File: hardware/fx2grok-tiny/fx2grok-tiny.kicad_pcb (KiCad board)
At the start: 2 copper layers, 13 x 13 mm, 28 parts, among them IC1 CY7C68013A-56, P1 CONN_01X05, P2 CONN_01X05, U1 MICRO-USB-B-SMD, U2 MIC5319, Y1 24MHz

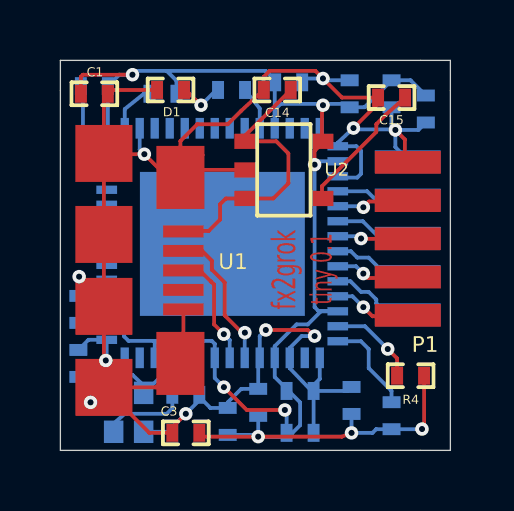
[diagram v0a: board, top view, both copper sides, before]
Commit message: Use rounded PCB edges, minor other improvements.
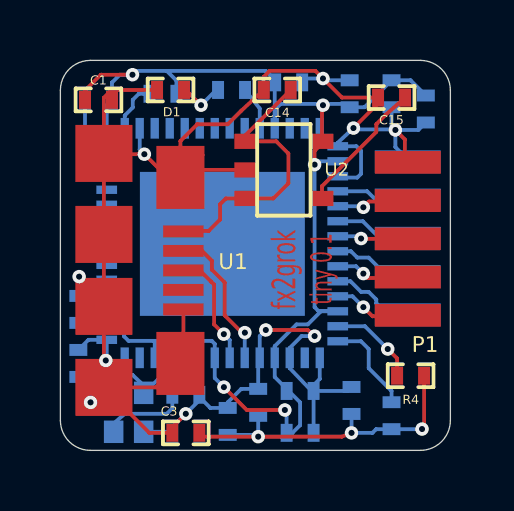
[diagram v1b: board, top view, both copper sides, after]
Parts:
- moved R1 0.48 mm to (69.0, 39.1)
- moved C1 0.25 mm to (69.0, 39.1)
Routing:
- net /WAKEUP: track 3.18 -> 2.63 mm
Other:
- outline, holes or cut-outs redrawn

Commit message: Add 0/1/GND pin markings on the 5x2 1.27mm connector.
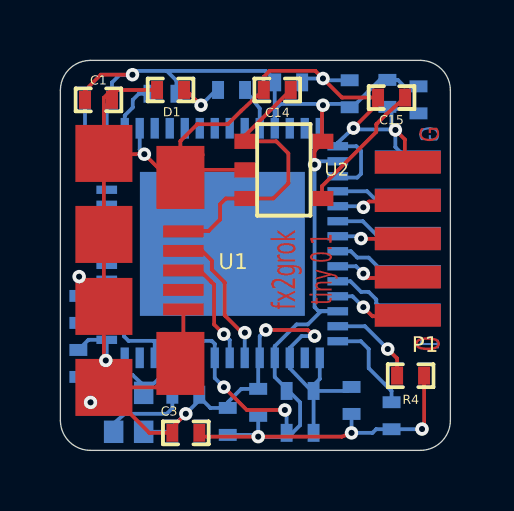
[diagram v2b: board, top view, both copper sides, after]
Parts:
- moved C16 0.39 mm to (79.6, 39.1)
- moved C10 0.14 mm to (78.6, 38.8)
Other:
- board text added: "0"
- board text added: "1"
- board text added: "G"
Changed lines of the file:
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@@
     (links 85)
     (no_connects 0)
-    (area 50.03038 32.773983 88.390762 61.842831)
+    (area 67.688459 37.736499 80.713861 50.761901)
     (thickness 0.8)
-    (drawings 12)
-    (tracks 346)
+    (drawings 16)
+    (tracks 356)
     (zones 0)
     (modules 28)
@@
   )
   (module SM0402 (layer B.Cu)
-    (at 79.883 39.37 270)
+    (at 79.63916 39.0652 270)
     (attr smd)
     (fp_text reference C16 (at -1.1108 0.11184 540) (layer B.SilkS)
@@
   )
   (module SM0402 (layer B.Cu)
-    (at 78.74 38.862 270)
+    (at 78.60116 38.8492 270)
     (attr smd)
     (fp_text reference C10 (at 1.56972 -0.02032 360) (layer B.SilkS)
@@
     (pad 5 smd rect (at 2.921 0.16002 90) (size 0.75946 2.2003) (layers F.Cu F.Paste F.Mask)
       (net 19 GND) (clearance 0.0508))
+  )
+  (gr_text G (at 80.02016 40.2082 90) (layer B.Cu)
+    (effects (font (size 0.635 0.508) (thickness 0.127)) (justify mirror))
+  )
+  (gr_text 1 (at 80.02016 47.1932 90) (layer B.Cu)
+    (effects (font (size 0.635 0.508) (thickness 0.127)) (justify mirror))
+  )
+  (gr_text G (at 80.02016 40.2082 90) (layer F.Cu)
+    (effects (font (size 0.635 0.508) (thickness 0.127)))
+  )
+  (gr_text 0 (at 79.96936 47.1932 90) (layer F.Cu)
+    (effects (font (size 0.802 0.624) (thickness 0.127)))
   )
   (dimension 13 (width 0.2048) (layer Dwgs.User)
@@
   (segment (start 70.4977 48.8315) (end 71.34606 48.00092) (width 0.127) (layer B.Cu) (net 18) (status 30))
   (segment (start 71.34606 48.00092) (end 71.34606 47.6631) (width 0.127) (layer B.Cu) (net 18) (status 30))
+  (segment (start 78.60116 39.29878) (end 78.67238 39.37) (width 0.127) (layer B.Cu) (net 19) (status C00000))
+  (segment (start 78.67238 39.37) (end 79.49438 39.37) (width 0.127) (layer B.Cu) (net 19) (status C00000))
+  (segment (start 79.49438 39.37) (end 79.63916 39.51478) (width 0.127) (layer B.Cu) (net 19) (status C00000))
+  (segment (start 79.58074 39.5732) (end 79.63916 39.51478) (width 0.127) (layer B.Cu) (net 19))
+  (segment (start 79.58074 39.5732) (end 79.63916 39.51478) (width 0.127) (layer B.Cu) (net 19))
   (segment (start 69.1515 43.55084) (end 69.1515 40.85082) (width 0.127) (layer F.Cu) (net 19))
   (segment (start 77.343 38.41242) (end 76.51242 38.41242) (width 0.127) (layer B.Cu) (net 19) (status 10))
@@
   (segment (start 77.47 40.05072) (end 77.47 40.005) (width 0.127) (layer B.Cu) (net 19))
   (segment (start 77.47 40.005) (end 77.47 40.05072) (width 0.127) (layer B.Cu) (net 19))
-  (segment (start 78.82128 40.05072) (end 78.867 40.005) (width 0.127) (layer B.Cu) (net 19))
+  (segment (start 78.82128 40.05072) (end 78.87716 39.99484) (width 0.127) (layer B.Cu) (net 19))
+  (segment (start 78.87716 39.99484) (end 78.87716 39.99484) (width 0.127) (layer B.Cu) (net 19))
+  (segment (start 78.87716 39.99484) (end 78.87716 39.99484) (width 0.127) (layer B.Cu) (net 19))
+  (segment (start 78.87716 39.99484) (end 78.87716 39.99484) (width 0.127) (layer B.Cu) (net 19))
+  (segment (start 78.87716 39.99484) (end 78.867 40.005) (width 0.127) (layer B.Cu) (net 19))
   (segment (start 78.867 40.0685) (end 78.867 40.005) (width 0.127) (layer B.Cu) (net 19))
   (segment (start 77.47 40.05072) (end 78.82128 40.05072) (width 0.127) (layer B.Cu) (net 19))
@@
   (segment (start 69.1515 38.99408) (end 69.1515 40.85082) (width 0.127) (layer F.Cu) (net 19) (status 30))
   (segment (start 74.48042 38.735) (end 74.48042 38.67658) (width 0.127) (layer F.Cu) (net 19) (status 30))
-  (segment (start 79.883 39.81958) (end 79.63408 40.0685) (width 0.127) (layer B.Cu) (net 19) (status 10))
-  (segment (start 79.63408 40.0685) (end 78.867 40.0685) (width 0.127) (layer B.Cu) (net 19))
   (segment (start 78.74 39.31158) (end 78.74 39.9415) (width 0.127) (layer B.Cu) (net 19) (status 10))
   (segment (start 78.74 39.9415) (end 78.867 40.0685) (width 0.127) (layer B.Cu) (net 19))
@@
   (segment (start 69.9516 41.65092) (end 69.1515 40.85082) (width 0.127) (layer F.Cu) (net 19) (status 30))
   (segment (start 69.2404 45.5676) (end 69.24548 45.56252) (width 0.127) (layer B.Cu) (net 19) (status 30))
+  (segment (start 78.60116 38.39962) (end 78.94818 38.39962) (width 0.127) (layer B.Cu) (net 20))
+  (segment (start 79.16418 38.61562) (end 79.63916 38.61562) (width 0.127) (layer B.Cu) (net 20))
+  (segment (start 78.94818 38.39962) (end 79.16418 38.61562) (width 0.127) (layer B.Cu) (net 20))
+  (segment (start 77.343 39.31158) (end 77.43698 39.31158) (width 0.127) (layer B.Cu) (net 20))
+  (segment (start 77.43698 39.31158) (end 78.34894 38.39962) (width 0.127) (layer B.Cu) (net 20))
+  (segment (start 78.34894 38.39962) (end 78.60116 38.39962) (width 0.127) (layer B.Cu) (net 20))
+  (segment (start 77.343 39.31158) (end 77.38618 39.31158) (width 0.127) (layer B.Cu) (net 20))
   (segment (start 69.42074 39.0652) (end 69.24548 39.24046) (width 0.127) (layer B.Cu) (net 20))
   (segment (start 69.24548 39.24046) (end 69.24548 40.61206) (width 0.127) (layer B.Cu) (net 20))
@@
   (segment (start 74.84618 40.01262) (end 74.84618 38.49624) (width 0.127) (layer B.Cu) (net 20) (status 30))
   (segment (start 74.84618 38.49624) (end 74.86142 38.481) (width 0.127) (layer B.Cu) (net 20) (status 30))
-  (segment (start 77.343 39.31158) (end 77.84084 39.31158) (width 0.127) (layer B.Cu) (net 20) (status 10))
-  (segment (start 77.84084 39.31158) (end 78.74 38.41242) (width 0.127) (layer B.Cu) (net 20) (status 20))
-  (segment (start 79.883 38.92042) (end 79.375 38.41242) (width 0.127) (layer B.Cu) (net 20) (status 10))
-  (segment (start 79.375 38.41242) (end 78.74 38.41242) (width 0.127) (layer B.Cu) (net 20) (status 20))
   (segment (start 76.42098 40.44696) (end 76.42098 39.27602) (width 0.127) (layer F.Cu) (net 20) (status 10))
   (via (at 76.454 39.243) (size 0.44958) (drill 0.20066) (layers F.Cu B.Cu) (net 20))
